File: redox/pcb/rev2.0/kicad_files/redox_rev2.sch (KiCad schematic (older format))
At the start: 146 parts, among them J2 OLED-SSD1306, K1 KEYSW, K10 KEYSW, K11 KEYSW, K12 KEYSW, K13 KEYSW, K14 KEYSW, K15 KEYSW, K16 KEYSW, K17 KEYSW, K18 KEYSW, K19 KEYSW, K2 KEYSW, K20 KEYSW, K21 KEYSW, K22 KEYSW, K23 KEYSW, K24 KEYSW, K25 KEYSW, K26 KEYSW, K27 KEYSW, K28 KEYSW, K29 KEYSW, K3 KEYSW, K30 KEYSW, K31 KEYSW, K32 KEYSW, K33 KEYSW, K34 KEYSW, K35 KEYSW, K4 KEYSW, K5 KEYSW, K6 KEYSW, K7 KEYSW, K8 KEYSW, K9 KEYSW, P1 TC2030-AVR, Q1 2N7002, U1 PRTR5V0U2X, U2 ATmega32U4, Y1 16Mhz

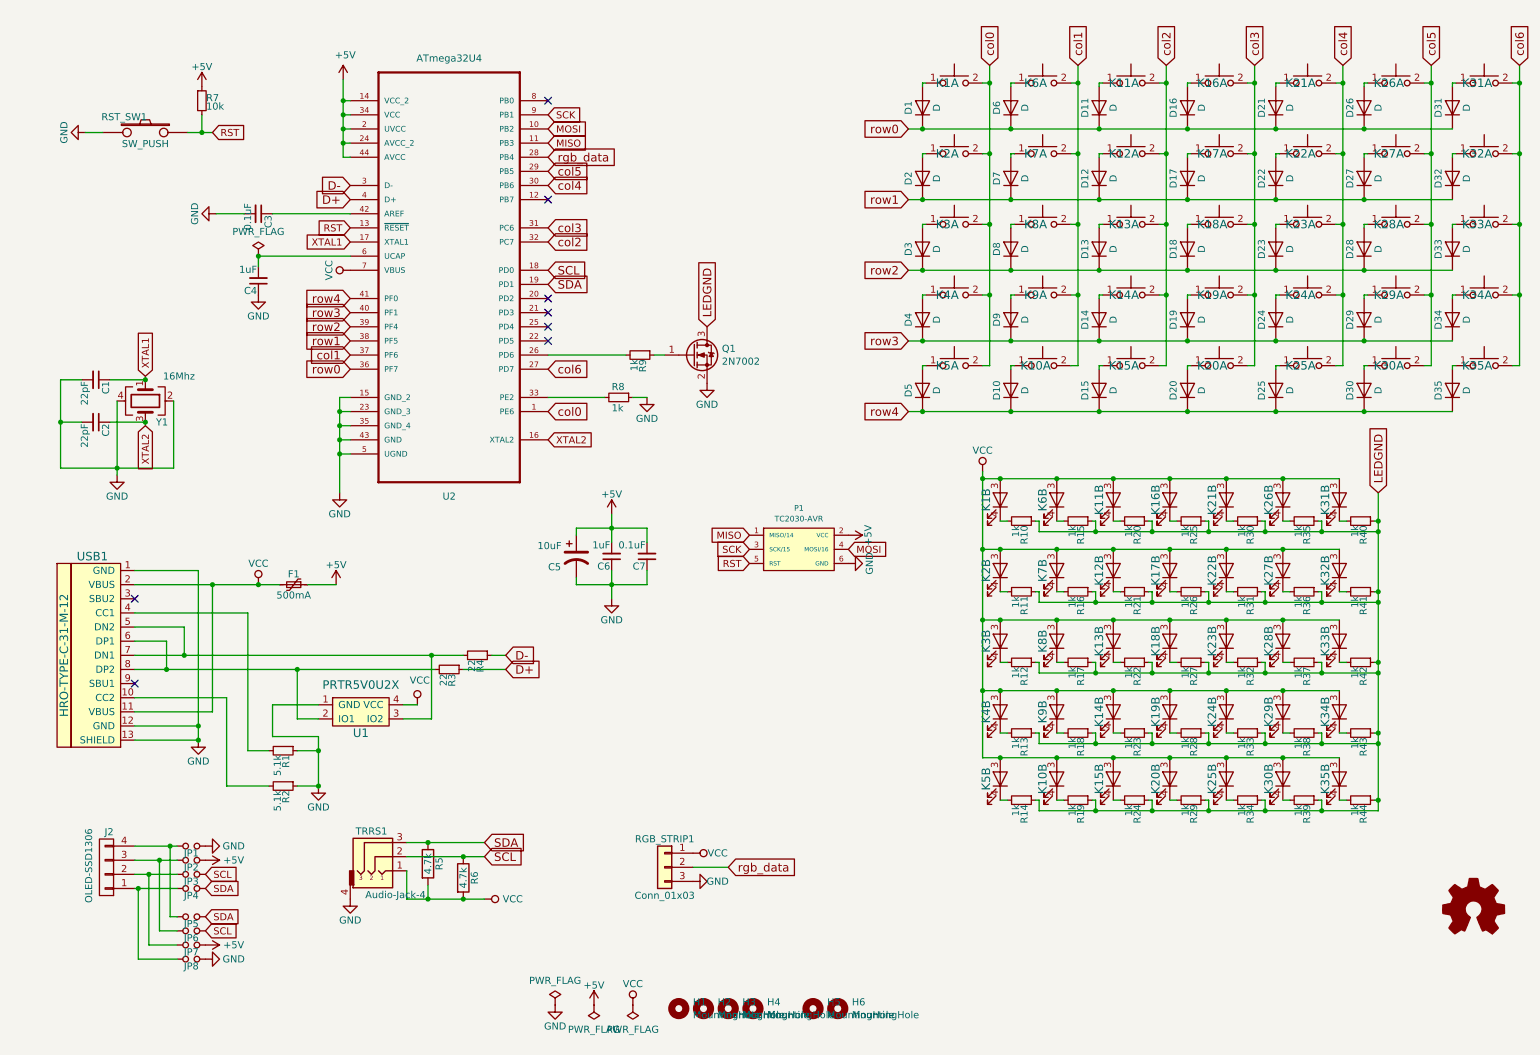
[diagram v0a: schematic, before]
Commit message: Schematic correction : replace VCC by VBUS and +5V by VCC, some other minor changes
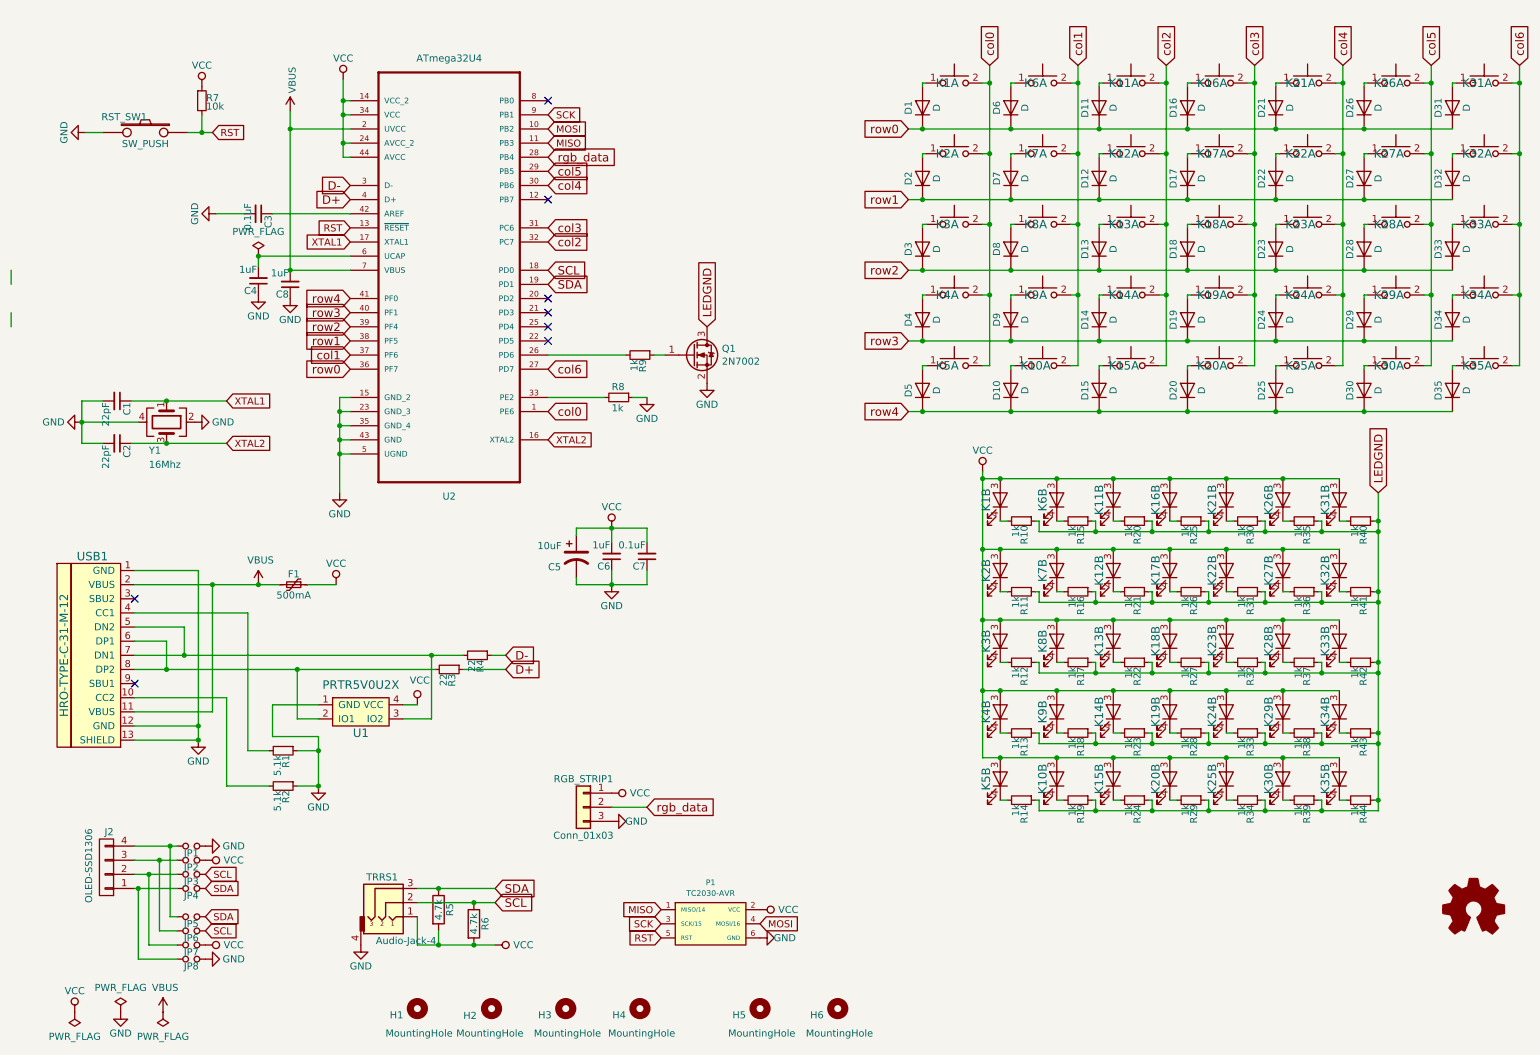
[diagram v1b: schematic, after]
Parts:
- added C8: 1uF, Keebio-Parts:C_0603, symbol Device:C_Small
- K30, K32, K35: footprint redox_footprints:Mx_Alps_125-dualside_with_LED -> redox_footprints:Mx_Alps_150-dualsided_with_LED
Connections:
- net GND: now also C8.1
- net VCC: now also C5.1, C6.2, C7.2, F1.1, JP2.2, JP7.2, P1.2 (VCC), R7.1, U2.14 (VCC_2), U2.24 (AVCC_2), U2.34 (VCC), U2.44 (AVCC); no longer F1.2, U2.7 (VBUS), USB1.11 (VBUS), USB1.2 (VBUS)
- removed net +5V: C5.1, C6.2, C7.2, F1.1, JP2.2, JP7.2, P1.2 (VCC), R7.1, U2.14 (VCC_2), U2.2 (UVCC), U2.24 (AVCC_2), U2.34 (VCC), U2.44 (AVCC)
- new net VBUS: C8.2, F1.2, U2.2 (UVCC), U2.7 (VBUS), USB1.11 (VBUS), USB1.2 (VBUS)
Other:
- moved on the sheet: C1, C2, H1, H2, H3, H4, H5, P1, R5, R6, RGB_STRIP1, TRRS1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
